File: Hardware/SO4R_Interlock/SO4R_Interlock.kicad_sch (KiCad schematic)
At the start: 165 parts, among them J1 12V, J2 USB-C 2.0 16P, J3 USB-C 2.0 16P, J4 USB-C 2.0 16P, J5 USB-C 2.0 16P, J6 Header 1x3, J7 RJ45_LED_Shielded, J8 8P8C_LED_Shielded_x4, Q1 2N7002, Q2 2N7002, Q3 2N7002, Q4 2N7002, U1 FT230XS, U10 TPD4E02B04DQA, U11 TPD4E02B04DQA, U12 TPD4E02B04DQA, U13 TPD4E02B04DQA, U2 FT230XS, U3 FT230XS, U4 FT230XS, U5 74LVC1G07, U6 74LVC1G07, U7 74LVC1G07, U8 BTS5200-4EKA, U9 AVR32DB48x-xPT

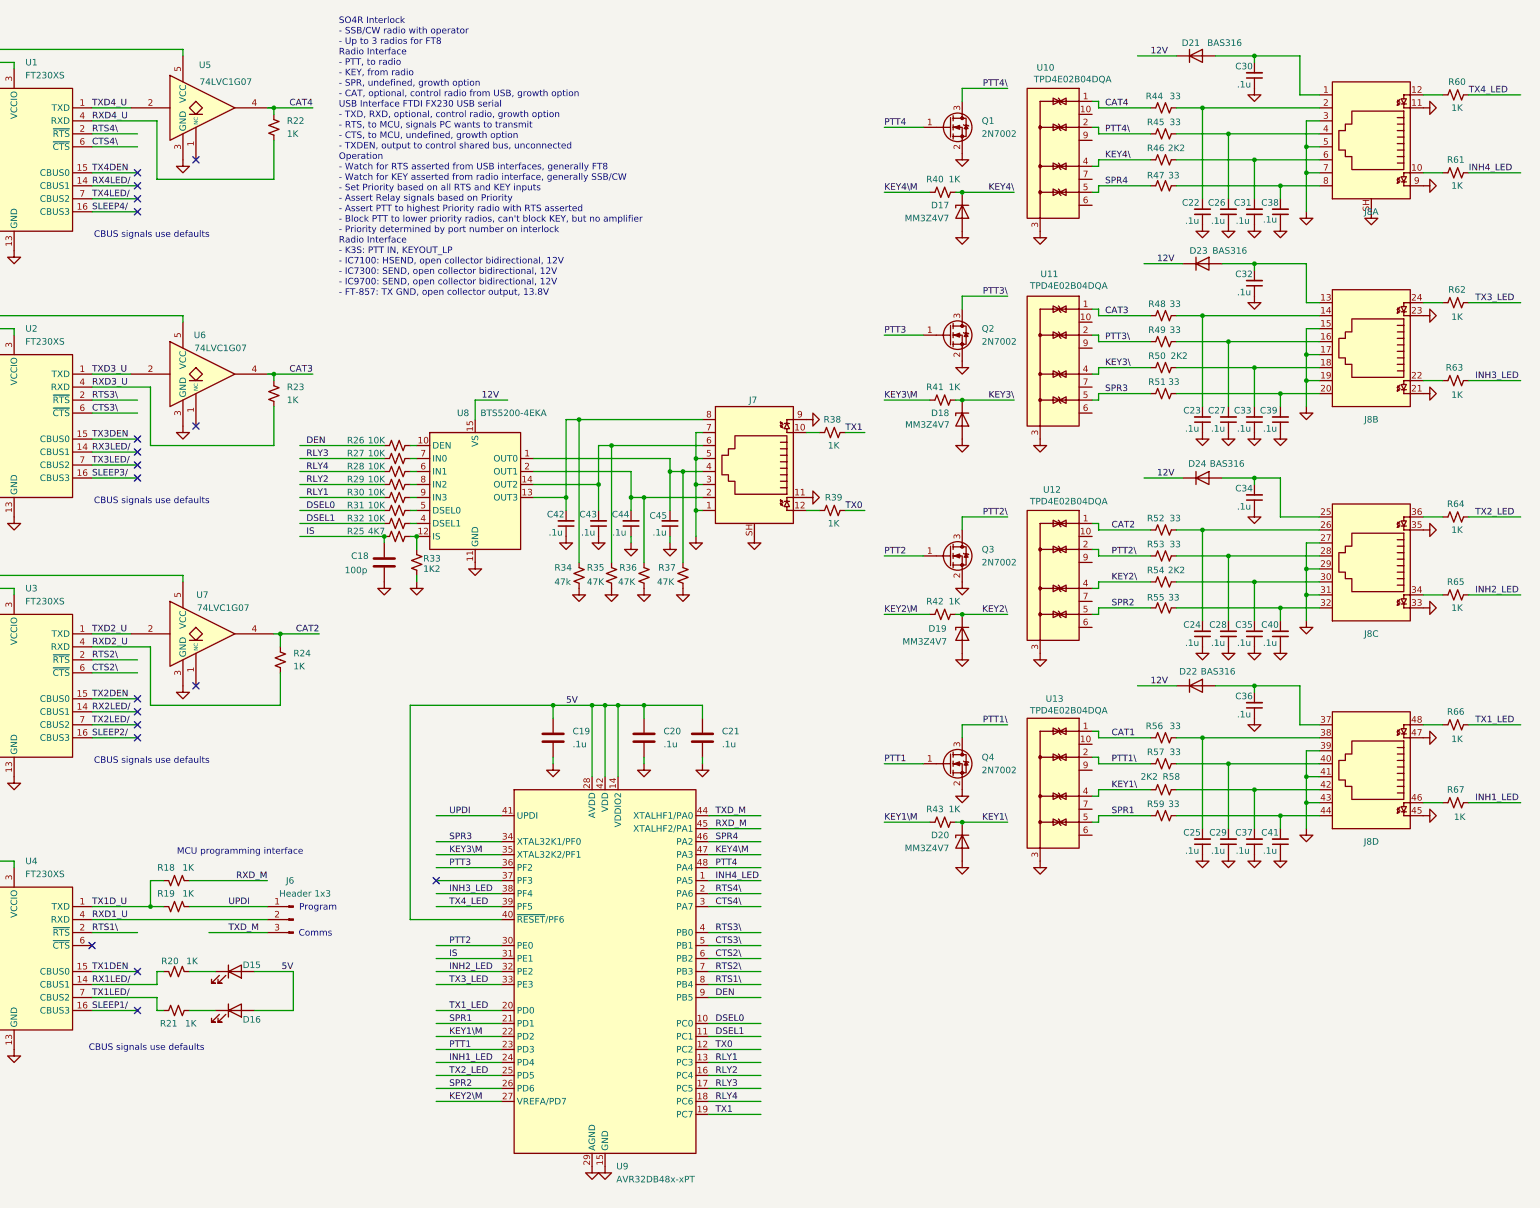
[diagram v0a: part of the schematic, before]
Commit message: Renamed LED signals for clarity Matching changes in Software and Hardware name
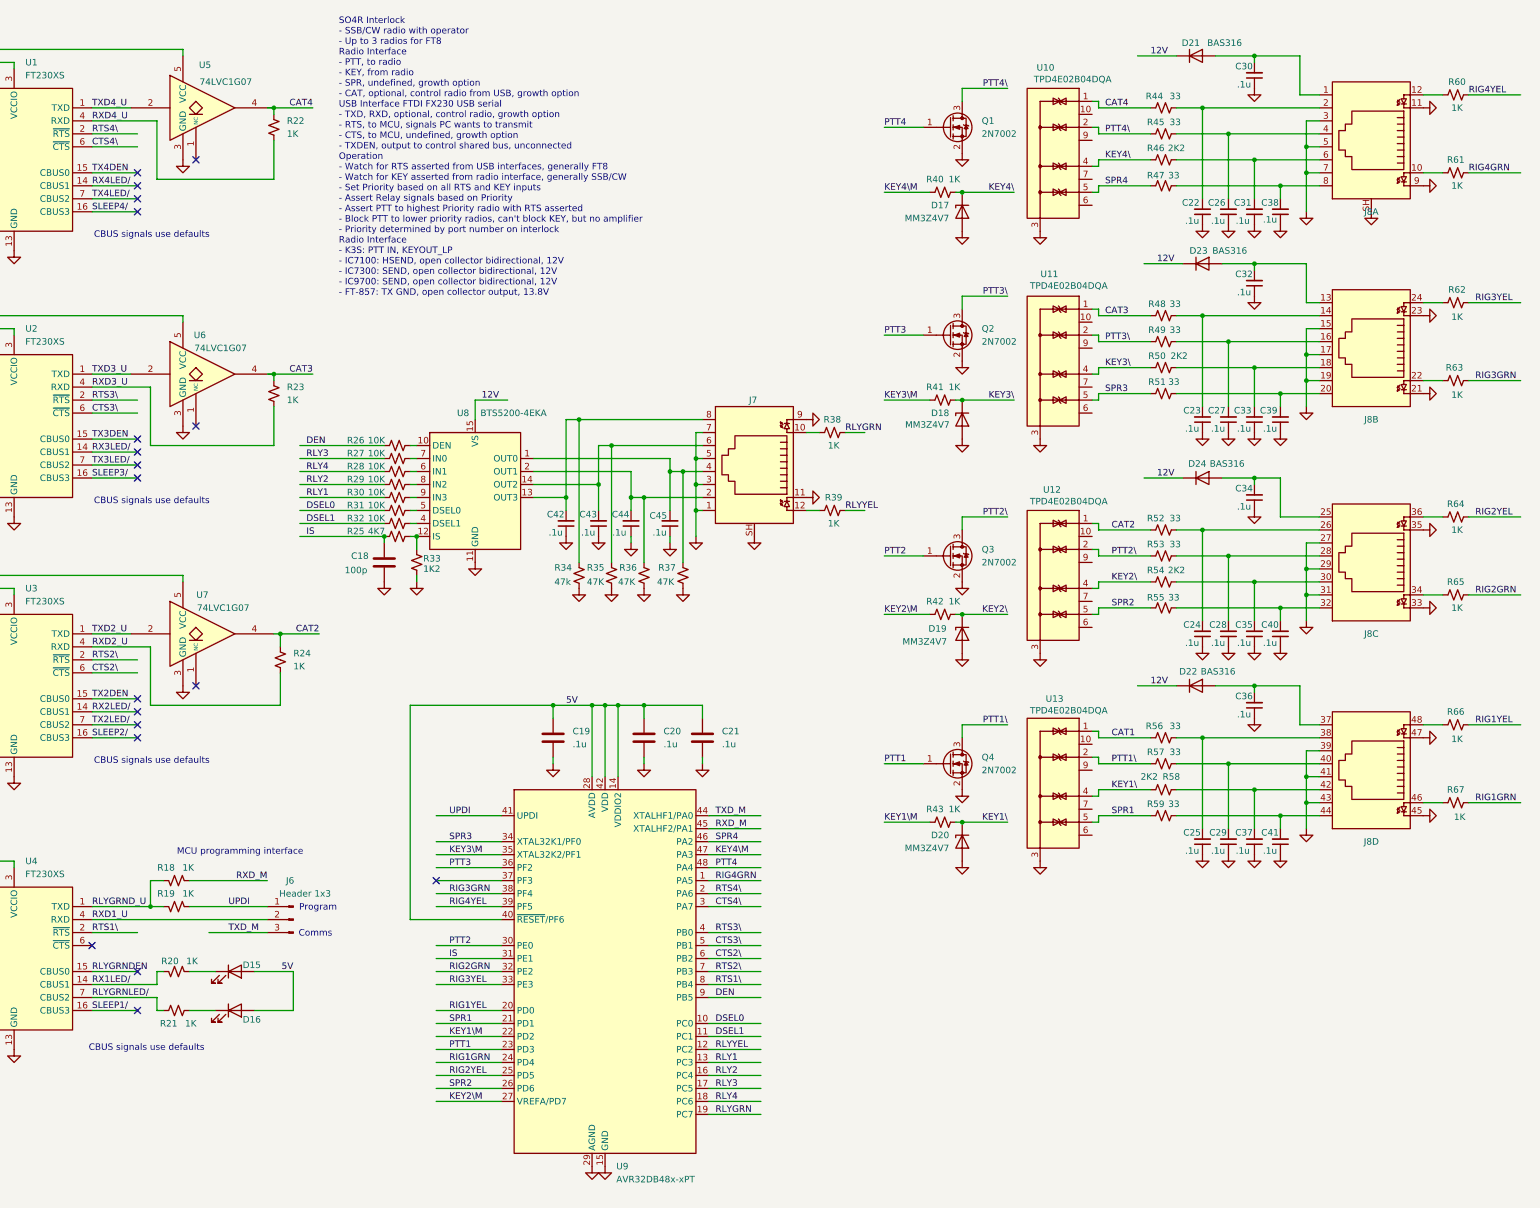
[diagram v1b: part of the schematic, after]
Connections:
- net INH1_LED renamed RIG1GRN
- net INH2_LED renamed RIG2GRN
- net INH3_LED renamed RIG3GRN
- net INH4_LED renamed RIG4GRN
- net TX0 renamed RLYYEL
- net TX1 renamed RLYGRN
- net TX1DEN renamed RLYGRNDEN
- net TX1D_U renamed RLYGRND_U
- net TX1LED/ renamed RLYGRNLED/
- net TX1_LED renamed RIG1YEL
- net TX2_LED renamed RIG2YEL
- net TX3_LED renamed RIG3YEL
- net TX4_LED renamed RIG4YEL
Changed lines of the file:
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@@
 		)
 	)
-	(label "TX1D_U"
+	(label "RLYGRND_U"
 		(at 138.43 190.5 0)
 		(effects
@@
 		)
 	)
-	(label "TX2_LED"
+	(label "RIG2YEL"
 		(at 408.94 114.3 0)
 		(effects
@@
 		)
 	)
-	(label "TX0"
+	(label "RLYYEL"
 		(at 285.75 113.03 0)
 		(effects
@@
 		)
 	)
-	(label "INH2_LED"
+	(label "RIG2GRN"
 		(at 208.28 203.2 0)
 		(effects
@@
 		)
 	)
-	(label "TX0"
+	(label "RLYYEL"
 		(at 260.35 218.44 0)
 		(effects
@@
 		)
 	)
-	(label "INH4_LED"
+	(label "RIG4GRN"
 		(at 260.35 185.42 0)
 		(effects
@@
 		)
 	)
-	(label "TX1"
+	(label "RLYGRN"
 		(at 285.75 97.79 0)
 		(effects
@@
 		)
 	)
-	(label "TX3_LED"
+	(label "RIG3YEL"
 		(at 208.28 205.74 0)
 		(effects
@@
 		)
 	)
-	(label "TX1DEN"
+	(label "RLYGRNDEN"
 		(at 138.43 203.2 0)
 		(effects
@@
 		)
 	)
-	(label "INH4_LED"
+	(label "RIG4GRN"
 		(at 407.67 46.99 0)
 		(effects
@@
 		)
 	)
-	(label "INH3_LED"
+	(label "RIG3GRN"
 		(at 408.94 87.63 0)
 		(effects
@@
 		)
 	)
-	(label "TX4_LED"
+	(label "RIG4YEL"
 		(at 407.67 31.75 0)
 		(effects
@@
 		)
 	)
-	(label "TX1_LED"
+	(label "RIG1YEL"
 		(at 208.28 210.82 0)
 		(effects
@@
 		)
 	)
-	(label "TX1"
+	(label "RLYGRN"
 		(at 260.35 231.14 0)
 		(effects
@@
 		)
 	)
-	(label "TX4_LED"
+	(label "RIG4YEL"
 		(at 208.28 190.5 0)
 		(effects
@@
 		)
 	)
-	(label "TX2_LED"
+	(label "RIG2YEL"
 		(at 208.28 223.52 0)
 		(effects
@@
 		)
 	)
-	(label "INH1_LED"
+	(label "RIG1GRN"
 		(at 408.94 170.18 0)
 		(effects
@@
 		)
 	)
-	(label "TX1LED/"
+	(label "RLYGRNLED/"
 		(at 138.43 208.28 0)
 		(effects
@@
 		)
 	)
-	(label "INH2_LED"
+	(label "RIG2GRN"
 		(at 408.94 129.54 0)
 		(effects
@@
 		)
 	)
-	(label "INH3_LED"
+	(label "RIG3GRN"
 		(at 208.28 187.96 0)
 		(effects
@@
 		)
 	)
-	(label "INH1_LED"
+	(label "RIG1GRN"
 		(at 208.28 220.98 0)
 		(effects
@@
 		)
 	)
-	(label "TX3_LED"
+	(label "RIG3YEL"
 		(at 408.94 72.39 0)
 		(effects
@@
 		)
 	)
-	(label "TX1_LED"
+	(label "RIG1YEL"
 		(at 408.94 154.94 0)
 		(effects

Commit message: still laying out pcb
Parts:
- removed D21, D22, D23, D24, D5: BAS316, Diode_SMD:D_SOD-323, symbol Diode:BAS316
- removed J2, J3, J4, J5: USB-C 2.0 16P, Interlock:USB_C_Receptacle_G-Switch_GT-USB-7010ASV, symbol Connector:USB_C_Receptacle_USB2.0_16P
- removed J6: Header 1x3, Connector_PinHeader_2.54mm:PinHeader_1x03_P2.54mm_Vertical, symbol Connector:Conn_01x03_Pin
- removed J8: 8P8C_LED_Shielded_x4, Connector_RJ:RJ45_Amphenol_RJHSE538X-04, symbol Interlock:8P8C_LED_Shielded_x4
- removed U10, U11, U12, U13: TPD4E02B04DQA, Package_SON:USON-10_2.5x1.0mm_P0.5mm, symbol Power_Protection:TPD4E02B04DQA
- added C26: .1u, Capacitor_SMD_Silkscreen:C_0402_1005Metric, symbol Device:C_Small
- added D1, D37, D38, D39, D40: RBQ161QS-40, Diode_SMD:D_0402_1005Metric, symbol Device:D_Schottky
- added D10: Green, LED_SMD:LED_0603_1608Metric, symbol Device:LED
- added D16, D17, D18, D19, D20, D21, D22, D23, D29, D30, D31, D32: Green, LED_SMD:LED_0805_2012Metric, symbol Device:LED
- added D26, D27, D28: MM3Z5V1, Diode_SMD:D_SOD-323F, symbol Diode:MM3Zxx
- added J2: USB_C_stacked, Interlock:CU3616SASCLA004-LF, symbol Interlock:USB-C_Stacked
- added J3: ~, Interlock:CU3616SASCLA004-LF, symbol Interlock:USB-C_Stacked
- added J5: Conn_Coaxial, Interlock:KLPX-0848A-2-B_KYC, symbol Connector:Conn_Coaxial
- added J6: 2041376-2, 2041376-2:TE_2041376-2, symbol RJ45_stacked_2x2_TE_2041376-2:2041376-2
- added Q1: 2N7002, Package_TO_SOT_SMD:SOT-23, symbol Transistor_FET:2N7002
- added R11, R12, R13, R14, R23, R24, R25, R26, R31, R32, R33, R34, R9: 1K, Resistor_SMD_Silkscreen:R_0402_1005Metric, symbol Device:R_Small_US
- added R35, R37, R39, R41: 4K7, Resistor_SMD_Silkscreen:R_0402_1005Metric, symbol Device:R_Small_US
- added R55: 33, Resistor_SMD_Silkscreen:R_0402_1005Metric, symbol Device:R_Small_US
- added SW1: SW_Wuerth_450301014042, Button_Switch_THT:SW_Slide-03_Wuerth-WS-SLTV_10x2.5x6.4_P2.54mm, symbol Switch:SW_Wuerth_450301014042
- C1, C14, C15, C16, C17, C18, C19: footprint Capacitor_SMD:C_0402_1005Metric -> Capacitor_SMD_Silkscreen:C_0402_1005Metric
- C10: renamed from C6; footprint Capacitor_SMD:C_0402_1005Metric -> Capacitor_SMD_Silkscreen:C_0402_1005Metric
- C11: renamed from C7; footprint Capacitor_SMD:C_0402_1005Metric -> Capacitor_SMD_Silkscreen:C_0402_1005Metric
- C12: renamed from C8; footprint Capacitor_SMD:C_0402_1005Metric -> Capacitor_SMD_Silkscreen:C_0402_1005Metric
- C13: renamed from C9; footprint Capacitor_SMD:C_0402_1005Metric -> Capacitor_SMD_Silkscreen:C_0402_1005Metric
- C2: renamed from C13; footprint Capacitor_SMD:C_0402_1005Metric -> Capacitor_SMD_Silkscreen:C_0402_1005Metric
- C20: renamed from C42; footprint Capacitor_SMD:C_0402_1005Metric -> Capacitor_SMD_Silkscreen:C_0402_1005Metric
- C21: renamed from C43; footprint Capacitor_SMD:C_0402_1005Metric -> Capacitor_SMD_Silkscreen:C_0402_1005Metric
- C22: renamed from C20; footprint Capacitor_SMD:C_0402_1005Metric -> Capacitor_SMD_Silkscreen:C_0402_1005Metric
- C23: renamed from C44; footprint Capacitor_SMD:C_0402_1005Metric -> Capacitor_SMD_Silkscreen:C_0402_1005Metric
- C24: renamed from C21; footprint Capacitor_SMD:C_0402_1005Metric -> Capacitor_SMD_Silkscreen:C_0402_1005Metric
- C25: renamed from C45; footprint Capacitor_SMD:C_0402_1005Metric -> Capacitor_SMD_Silkscreen:C_0402_1005Metric
- C27: renamed from C22; footprint Capacitor_SMD:C_0402_1005Metric -> Capacitor_SMD_Silkscreen:C_0402_1005Metric
- C28: renamed from C23; footprint Capacitor_SMD:C_0402_1005Metric -> Capacitor_SMD_Silkscreen:C_0402_1005Metric
- C29: renamed from C24; footprint Capacitor_SMD:C_0402_1005Metric -> Capacitor_SMD_Silkscreen:C_0402_1005Metric
- C3: renamed from C12; footprint Capacitor_SMD:C_0402_1005Metric -> Capacitor_SMD_Silkscreen:C_0402_1005Metric
- C30: renamed from C25; footprint Capacitor_SMD:C_0402_1005Metric -> Capacitor_SMD_Silkscreen:C_0402_1005Metric
- C31: renamed from C26; footprint Capacitor_SMD:C_0402_1005Metric -> Capacitor_SMD_Silkscreen:C_0402_1005Metric
- C32: renamed from C27; footprint Capacitor_SMD:C_0402_1005Metric -> Capacitor_SMD_Silkscreen:C_0402_1005Metric
- C33: renamed from C28; footprint Capacitor_SMD:C_0402_1005Metric -> Capacitor_SMD_Silkscreen:C_0402_1005Metric
- C34: renamed from C29; footprint Capacitor_SMD:C_0402_1005Metric -> Capacitor_SMD_Silkscreen:C_0402_1005Metric
- C35: renamed from C30; footprint Capacitor_SMD:C_0402_1005Metric -> Capacitor_SMD_Silkscreen:C_0402_1005Metric
- C36: renamed from C31; footprint Capacitor_SMD:C_0402_1005Metric -> Capacitor_SMD_Silkscreen:C_0402_1005Metric
- C37: renamed from C32; footprint Capacitor_SMD:C_0402_1005Metric -> Capacitor_SMD_Silkscreen:C_0402_1005Metric
- C38: renamed from C33; footprint Capacitor_SMD:C_0402_1005Metric -> Capacitor_SMD_Silkscreen:C_0402_1005Metric
- C39: renamed from C34; footprint Capacitor_SMD:C_0402_1005Metric -> Capacitor_SMD_Silkscreen:C_0402_1005Metric
- C4: renamed from C10; footprint Capacitor_SMD:C_0402_1005Metric -> Capacitor_SMD_Silkscreen:C_0402_1005Metric
- C40: renamed from C35; footprint Capacitor_SMD:C_0402_1005Metric -> Capacitor_SMD_Silkscreen:C_0402_1005Metric
- C41: renamed from C36; footprint Capacitor_SMD:C_0402_1005Metric -> Capacitor_SMD_Silkscreen:C_0402_1005Metric
- C42: renamed from C37; footprint Capacitor_SMD:C_0402_1005Metric -> Capacitor_SMD_Silkscreen:C_0402_1005Metric
- C43: renamed from C38; footprint Capacitor_SMD:C_0402_1005Metric -> Capacitor_SMD_Silkscreen:C_0402_1005Metric
- C44: renamed from C39; footprint Capacitor_SMD:C_0402_1005Metric -> Capacitor_SMD_Silkscreen:C_0402_1005Metric
- C45: renamed from C40; footprint Capacitor_SMD:C_0402_1005Metric -> Capacitor_SMD_Silkscreen:C_0402_1005Metric
- C46: renamed from C41; footprint Capacitor_SMD:C_0402_1005Metric -> Capacitor_SMD_Silkscreen:C_0402_1005Metric
- C5: renamed from C2; footprint Capacitor_SMD:C_0402_1005Metric -> Capacitor_SMD_Silkscreen:C_0402_1005Metric
- C6: renamed from C3; footprint Capacitor_SMD:C_0402_1005Metric -> Capacitor_SMD_Silkscreen:C_0402_1005Metric
- C7: renamed from C4; footprint Capacitor_SMD:C_0402_1005Metric -> Capacitor_SMD_Silkscreen:C_0402_1005Metric
- C8: renamed from C5; footprint Capacitor_SMD:C_0402_1005Metric -> Capacitor_SMD_Silkscreen:C_0402_1005Metric
- C9: renamed from C11; footprint Capacitor_SMD:C_0402_1005Metric -> Capacitor_SMD_Silkscreen:C_0402_1005Metric
- D11: renamed from D10; footprint Diode_SMD:D_SOD-323 -> Diode_SMD:D_SOD-523
- D12: renamed from D11; footprint Diode_SMD:D_SOD-323 -> Diode_SMD:D_SOD-523
- D13: renamed from D12; footprint Diode_SMD:D_SOD-323 -> Diode_SMD:D_SOD-523
- D14: renamed from D13; footprint Diode_SMD:D_SOD-323 -> Diode_SMD:D_SOD-523
- D2: renamed from D1; footprint Diode_SMD:D_SOD-323 -> Diode_SMD:D_SOD-523
- D3: renamed from D2; footprint Diode_SMD:D_SOD-323 -> Diode_SMD:D_SOD-523
- D33: renamed from D17; value MM3Z4V7 -> MM3Z5V1; footprint Diode_SMD:D_SOD-323 -> Diode_SMD:D_SOD-523
- D34: renamed from D18; value MM3Z4V7 -> MM3Z5V1; footprint Diode_SMD:D_SOD-323 -> Diode_SMD:D_SOD-523
- D35: renamed from D19; value MM3Z4V7 -> MM3Z5V1; footprint Diode_SMD:D_SOD-323 -> Diode_SMD:D_SOD-523
- D36: renamed from D20; value MM3Z4V7 -> MM3Z5V1; footprint Diode_SMD:D_SOD-323 -> Diode_SMD:D_SOD-523
- D4: renamed from D3; footprint Diode_SMD:D_SOD-323 -> Diode_SMD:D_SOD-523
- D5: renamed from D4; footprint Diode_SMD:D_SOD-323 -> Diode_SMD:D_SOD-523
- R1: footprint Resistor_SMD:R_0402_1005Metric -> Resistor_SMD_Silkscreen:R_0402_1005Metric; symbol Device:R_US -> Device:R_Small_US
- R10: renamed from R9; footprint Resistor_SMD:R_0402_1005Metric -> Resistor_SMD_Silkscreen:R_0402_1005Metric
- R15: renamed from R10; footprint Resistor_SMD:R_0402_1005Metric -> Resistor_SMD_Silkscreen:R_0402_1005Metric
- R16: renamed from R11; footprint Resistor_SMD:R_0402_1005Metric -> Resistor_SMD_Silkscreen:R_0402_1005Metric
- R17: renamed from R12; footprint Resistor_SMD:R_0402_1005Metric -> Resistor_SMD_Silkscreen:R_0402_1005Metric
- R18: renamed from R13; footprint Resistor_SMD:R_0402_1005Metric -> Resistor_SMD_Silkscreen:R_0402_1005Metric
- R19: renamed from R14; footprint Resistor_SMD:R_0402_1005Metric -> Resistor_SMD_Silkscreen:R_0402_1005Metric
- R2, R3, R4, R5, R6, R7, R8: footprint Resistor_SMD:R_0402_1005Metric -> Resistor_SMD_Silkscreen:R_0402_1005Metric
- R20: renamed from R15; footprint Resistor_SMD:R_0402_1005Metric -> Resistor_SMD_Silkscreen:R_0402_1005Metric
- R21: renamed from R16; footprint Resistor_SMD:R_0402_1005Metric -> Resistor_SMD_Silkscreen:R_0402_1005Metric
- R22: renamed from R17; footprint Resistor_SMD:R_0402_1005Metric -> Resistor_SMD_Silkscreen:R_0402_1005Metric
- R27: renamed from R18; footprint Resistor_SMD:R_0402_1005Metric -> Resistor_SMD_Silkscreen:R_0402_1005Metric
- R28: renamed from R19; footprint Resistor_SMD:R_0402_1005Metric -> Resistor_SMD_Silkscreen:R_0402_1005Metric
- R29: renamed from R20; footprint Resistor_SMD:R_0402_1005Metric -> Resistor_SMD_Silkscreen:R_0402_1005Metric
- R30: renamed from R21; footprint Resistor_SMD:R_0402_1005Metric -> Resistor_SMD_Silkscreen:R_0402_1005Metric
- R36: renamed from R22; value 1K -> 4K7; footprint Resistor_SMD:R_0402_1005Metric -> Resistor_SMD_Silkscreen:R_0402_1005Metric
- R38: renamed from R23; value 1K -> 4K7; footprint Resistor_SMD:R_0402_1005Metric -> Resistor_SMD_Silkscreen:R_0402_1005Metric
- R40: renamed from R24; value 1K -> 4K7; footprint Resistor_SMD:R_0402_1005Metric -> Resistor_SMD_Silkscreen:R_0402_1005Metric
- R42: renamed from R26; footprint Resistor_SMD:R_0402_1005Metric -> Resistor_SMD_Silkscreen:R_0402_1005Metric
- R43: renamed from R27; footprint Resistor_SMD:R_0402_1005Metric -> Resistor_SMD_Silkscreen:R_0402_1005Metric
- R44: renamed from R28; footprint Resistor_SMD:R_0402_1005Metric -> Resistor_SMD_Silkscreen:R_0402_1005Metric
- R45: renamed from R29; footprint Resistor_SMD:R_0402_1005Metric -> Resistor_SMD_Silkscreen:R_0402_1005Metric
- R46: renamed from R30; footprint Resistor_SMD:R_0402_1005Metric -> Resistor_SMD_Silkscreen:R_0402_1005Metric
- R47: renamed from R31; footprint Resistor_SMD:R_0402_1005Metric -> Resistor_SMD_Silkscreen:R_0402_1005Metric
- R48: renamed from R32; footprint Resistor_SMD:R_0402_1005Metric -> Resistor_SMD_Silkscreen:R_0402_1005Metric
- R49: renamed from R25; footprint Resistor_SMD:R_0402_1005Metric -> Resistor_SMD_Silkscreen:R_0402_1005Metric
- R50: renamed from R33; footprint Resistor_SMD:R_0402_1005Metric -> Resistor_SMD_Silkscreen:R_0402_1005Metric
- R51: renamed from R34; value 47k -> 4K7; footprint Resistor_SMD:R_0402_1005Metric -> Resistor_SMD_Silkscreen:R_0402_1005Metric
- R52: renamed from R35; footprint Resistor_SMD:R_0402_1005Metric -> Resistor_SMD_Silkscreen:R_0402_1005Metric
- R53: renamed from R36; footprint Resistor_SMD:R_0402_1005Metric -> Resistor_SMD_Silkscreen:R_0402_1005Metric
- R54: renamed from R37; footprint Resistor_SMD:R_0402_1005Metric -> Resistor_SMD_Silkscreen:R_0402_1005Metric
- R56: renamed from R38; footprint Resistor_SMD:R_0402_1005Metric -> Resistor_SMD_Silkscreen:R_0402_1005Metric
- R57: renamed from R39; footprint Resistor_SMD:R_0402_1005Metric -> Resistor_SMD_Silkscreen:R_0402_1005Metric
- R58: renamed from R40; footprint Resistor_SMD:R_0402_1005Metric -> Resistor_SMD_Silkscreen:R_0402_1005Metric
- R59: renamed from R41; footprint Resistor_SMD:R_0402_1005Metric -> Resistor_SMD_Silkscreen:R_0402_1005Metric
- R60: renamed from R42; footprint Resistor_SMD:R_0402_1005Metric -> Resistor_SMD_Silkscreen:R_0402_1005Metric
- R61: renamed from R43; footprint Resistor_SMD:R_0402_1005Metric -> Resistor_SMD_Silkscreen:R_0402_1005Metric
- R62: renamed from R44; footprint Resistor_SMD:R_0402_1005Metric -> Resistor_SMD_Silkscreen:R_0402_1005Metric
- R63: renamed from R45; footprint Resistor_SMD:R_0402_1005Metric -> Resistor_SMD_Silkscreen:R_0402_1005Metric
- R64: renamed from R46; footprint Resistor_SMD:R_0402_1005Metric -> Resistor_SMD_Silkscreen:R_0402_1005Metric
- R65: renamed from R47; footprint Resistor_SMD:R_0402_1005Metric -> Resistor_SMD_Silkscreen:R_0402_1005Metric
- R66: renamed from R48; footprint Resistor_SMD:R_0402_1005Metric -> Resistor_SMD_Silkscreen:R_0402_1005Metric
- R67: renamed from R49; footprint Resistor_SMD:R_0402_1005Metric -> Resistor_SMD_Silkscreen:R_0402_1005Metric
- R68: renamed from R50; footprint Resistor_SMD:R_0402_1005Metric -> Resistor_SMD_Silkscreen:R_0402_1005Metric
- R69: renamed from R51; footprint Resistor_SMD:R_0402_1005Metric -> Resistor_SMD_Silkscreen:R_0402_1005Metric
- R70: renamed from R52; footprint Resistor_SMD:R_0402_1005Metric -> Resistor_SMD_Silkscreen:R_0402_1005Metric
- R71: renamed from R53; footprint Resistor_SMD:R_0402_1005Metric -> Resistor_SMD_Silkscreen:R_0402_1005Metric
- R72: renamed from R54; footprint Resistor_SMD:R_0402_1005Metric -> Resistor_SMD_Silkscreen:R_0402_1005Metric
- R73: renamed from R55; footprint Resistor_SMD:R_0402_1005Metric -> Resistor_SMD_Silkscreen:R_0402_1005Metric
- R74: renamed from R56; footprint Resistor_SMD:R_0402_1005Metric -> Resistor_SMD_Silkscreen:R_0402_1005Metric
- R75: renamed from R57; footprint Resistor_SMD:R_0402_1005Metric -> Resistor_SMD_Silkscreen:R_0402_1005Metric
- R76: renamed from R58; footprint Resistor_SMD:R_0402_1005Metric -> Resistor_SMD_Silkscreen:R_0402_1005Metric
- R77: renamed from R59; footprint Resistor_SMD:R_0402_1005Metric -> Resistor_SMD_Silkscreen:R_0402_1005Metric
- R78: renamed from R61; footprint Resistor_SMD:R_0402_1005Metric -> Resistor_SMD_Silkscreen:R_0402_1005Metric
- R79: renamed from R60; footprint Resistor_SMD:R_0402_1005Metric -> Resistor_SMD_Silkscreen:R_0402_1005Metric
- R80: renamed from R62; footprint Resistor_SMD:R_0402_1005Metric -> Resistor_SMD_Silkscreen:R_0402_1005Metric
- R81: renamed from R63; footprint Resistor_SMD:R_0402_1005Metric -> Resistor_SMD_Silkscreen:R_0402_1005Metric
- R82: renamed from R64; footprint Resistor_SMD:R_0402_1005Metric -> Resistor_SMD_Silkscreen:R_0402_1005Metric
- R83: renamed from R65; footprint Resistor_SMD:R_0402_1005Metric -> Resistor_SMD_Silkscreen:R_0402_1005Metric
- R84: renamed from R67; footprint Resistor_SMD:R_0402_1005Metric -> Resistor_SMD_Silkscreen:R_0402_1005Metric
- R85: renamed from R66; footprint Resistor_SMD:R_0402_1005Metric -> Resistor_SMD_Silkscreen:R_0402_1005Metric
- U8: footprint Interlock:Infineon_PG-DSO-14-48-EP -> Package_SO:Infineon_PG-DSO-14-48
- renumbered D14 to D15, D15 to D24, D16 to D25, D9 to D6, D6 to D7, D7 to D8, D8 to D9, J7 to J4, Q1 to Q2, Q2 to Q3, Q3 to Q4, Q4 to Q5
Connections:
- net 12V: now also D1.1 (K), D37.1 (K), D38.1 (K), D39.1 (K), D40.1 (K), R9.2
- net 5V: now also R11.1, R12.1, R13.1, R14.1, R35.1, R37.1, R39.1, R41.1; no longer U9.40 (~{RESET}/PF6)
- net CAT2: now also R39.2
- net CAT3: now also R37.2
- net CAT4: now also R35.2
- net CTS2\: now also U9.24 (PD4); no longer U9.6 (PB2)
- net CTS3\: now also U9.22 (PD2); no longer U9.5 (PB1)
- net CTS4\: now also U9.20 (PD0); no longer U9.3 (PA7)
- net DEN: now also U9.32 (PE2); no longer U9.9 (PB5)
- net DSEL0: now also U9.37 (PF3); no longer U9.10 (PC0)
- net DSEL1: now also U9.38 (PF4); no longer U9.11 (PC1)
- net GND: now also C26.1, D10.1 (K), D20.1 (K), D21.1 (K), D22.1 (K), D23.1 (K), D26.2 (A), D27.1 (K), D28.2 (A), D29.1 (K), D30.1 (K), D31.1 (K), D32.1 (K), J2.A12a (GND), J2.A12b (GND), J2.A1a (GND), J2.A1b (GND), J2.B12a (GND), J2.B12b (GND), J2.B1a (GND), J2.B1b (GND), J2.S1 (SHIELD), J3.A12a (GND), J3.A12b (GND), J3.A1a (GND), J3.A1b (GND), J3.B12a (GND), J3.B12b (GND), J3.B1a (GND), J3.B1b (GND), J3.S1 (SHIELD), J5.2 (Ext), J6.A3, J6.A5, J6.A7, J6.B3, J6.B5, J6.B7, J6.C3, J6.C5, J6.C7, J6.D3, J6.D5, J6.D7, J6.GK_A, J6.GK_B, J6.GK_C, J6.GK_D, J6.S1 (SHIELD), J6.S2 (SHIELD__1), J6.S3 (SHIELD__2), J6.S4 (SHIELD__3), J6.YK_A, J6.YK_B, J6.YK_C, J6.YK_D, Q1.2 (S)
- net KEY1\M: now also U9.11 (PC1); no longer U9.22 (PD2)
- net KEY2\M: now also U9.5 (PB1); no longer U9.27 (VREFA/PD7)
- net KEY3\M: now also U9.17 (PC5); no longer U9.35 (XTAL32K2/PF1)
- net KEY4\M: now also U9.1 (PA5); no longer U9.47 (PA3)
- net PTT1: now also U9.12 (PC2); no longer U9.23 (PD3)
- net PTT2: now also R82.2, U9.6 (PB2), R24.1; no longer U9.30 (PE0)
- net PTT3: now also R80.2, U9.16 (PC4), R25.1; no longer U9.36 (PF2)
- net PTT4: now also R78.2, R26.1
- net RIG1GRN: now also U9.8 (PB4), R23.1; no longer U9.24 (PD4)
- net RIG1YEL: now also U9.13 (PC3), R31.1; no longer U9.20 (PD0)
- net RIG2YEL: now also R83.2, U9.7 (PB3), R32.1; no longer R82.2, U9.25 (PD5)
- net RIG3YEL: now also R81.2, U9.19 (PC7), R33.1; no longer R80.2, U9.33 (PE3)
- net RIG4YEL: now also U9.46 (PA2), R34.1; no longer U9.39 (PF5)
- net RLY1: now also U9.33 (PE3); no longer U9.13 (PC3)
- net RLY2: now also U9.34 (XTAL32K1/PF0); no longer U9.16 (PC4)
- net RLY3: now also U9.35 (XTAL32K2/PF1); no longer U9.17 (PC5)
- net RLY4: now also U9.36 (PF2); no longer U9.18 (PC6)
- net RLYGRN: now also U9.39 (PF5); no longer U9.19 (PC7)
- net RLYYEL: now also U9.30 (PE0); no longer U9.12 (PC2)
- net RTS1\: now also U9.26 (PD6); no longer U9.8 (PB4)
- net RTS2\: now also U9.25 (PD5); no longer U9.7 (PB3)
- net RTS3\: now also U9.23 (PD3); no longer U9.4 (PB0)
- net RTS4\: now also U9.21 (PD1); no longer U9.2 (PA6)
- net RXD1_U: now also SW1.1 (B)
- net RXD2_U: now also D28.1 (K)
- net RXD3_U: now also D27.2 (A)
- net RXD4_U: now also D26.1 (K)
- net SPR1: now also U9.10 (PC0); no longer U9.21 (PD1)
- net SPR2: now also U9.4 (PB0); no longer U9.26 (PD6)
- net SPR3: now also U9.18 (PC6); no longer U9.34 (XTAL32K1/PF0)
- net SPR4: now also U9.2 (PA6); no longer U9.46 (PA2)
- net TXD_M: now also SW1.2 (C)
- net UPDI: now also SW1.3 (A)
- net at R3.2: now also J2.A5b (CC1)
- net at C28.2, R66.2: now also J6.B2
- net at C37.2: now also D39.2 (A), J6.B1
- net at C32.2, R67.2: now also J6.B4
- net at C38.2, R68.1: now also J6.B6
- net at C44.2, R69.2: now also J6.B8
- net at R81.1: now also J6.YA_B
- net at R80.1: now also J6.GA_B
- net at C8.1, D14.1 (K), R21.2: now also J3.A7b (D-), J3.B7b (D-)
- net at C1.1, J1.1 (In): now also D1.2 (A)
- net at C11.1, D3.1 (K), R18.2: now also J2.A6b (D+), J2.B6b (D+)
- net at C39.2: now also D40.2 (A), J6.C1
- net at C29.2, R70.2: now also J6.C2
- net at C33.2, R71.2: now also J6.C4
- net at C40.2, R72.1: now also J6.C6
- net at C45.2, R73.2: now also J6.C8
- net at R83.1: now also J6.YA_C
- net at R82.1: now also J6.GA_C
- net at C31.2, R63.2: now also J6.A4
- net at C30.2, R74.2: now also J6.D2
- net at C13.1, D5.1 (K), R22.2: now also J3.A6b (D+), J3.B6b (D+)
- net at C34.2, R75.2: now also J6.D4
- net at C5.1, D11.1 (K), R15.2: now also J2.A7a (D-), J2.B7a (D-)
- net at R1.2: now also J2.A5a (CC1)
- net at C43.2, R65.2: now also J6.A8
- net at C41.2: now also D38.2 (A), J6.D1
- net at R79.1: now also J6.YA_A
- net at FB1.1: now also J2.A4b (VBUS), J2.A9b (VBUS), J2.B4b (VBUS), J2.B9b (VBUS)
- net at C10.1, D2.1 (K), R16.2: now also J2.A6a (D+), J2.B6a (D+)
- net at C42.2, R76.1: now also J6.D6
- net at C6.1, D12.1 (K), R17.2: now also J2.A7b (D-), J2.B7b (D-)
- net at R4.2: now also J2.B5b (CC2)
- net at C12.1, D4.1 (K), R20.2: now also J3.A6a (D+), J3.B6a (D+)
- net at FB4.1: now also J2.A4a (VBUS), J2.A9a (VBUS), J2.B4a (VBUS), J2.B9a (VBUS)
- net at R2.2: now also J2.B5a (CC2)
- net at C46.2, R77.2: now also J6.D8
- net at R85.1: now also J6.YA_D
- net at C7.1, D13.1 (K), R19.2: now also J3.A7a (D-), J3.B7a (D-)
- net at C27.2, R62.2: now also J6.A2
- net at R8.2: now also J3.B5b (CC2)
- net at C35.2: now also D37.2 (A), J6.A1
- net at R84.1: now also J6.GA_D
- net at R78.1: now also J6.GA_A
- net at C36.2, R64.1: now also J6.A6
- net at R5.2: now also J3.A5a (CC1)
- net at FB2.1: now also J3.A4a (VBUS), J3.A9a (VBUS), J3.B4a (VBUS), J3.B9a (VBUS)
- net at R6.2: now also J3.B5a (CC2)
- net at FB3.1: now also J3.A4b (VBUS), J3.A9b (VBUS), J3.B4b (VBUS), J3.B9b (VBUS)
- net at R7.2: now also J3.A5b (CC1)
- removed net RIG2GRN: R83.2, U9.32 (PE2)
- removed net RIG3GRN: R81.2, U9.38 (PF4)
- removed net RIG4GRN: R78.2, U9.1 (PA5)
- net RLYGRNDEN renamed TX1DEN
- net RLYGRND_U renamed TXD1_U
- net RLYGRNLED/ renamed TX1LED/
- new net: D10.2 (A), R9.1
- new net: D29.2 (A), R31.2
- new net: D30.2 (A), R32.2
- new net: D18.2 (A), R13.2
- new net: D31.2 (A), R33.2
- new net: D22.2 (A), R25.2
- new net: D23.2 (A), R26.2
- new net: R41.2, U9.40 (~{RESET}/PF6)
- new net: D17.2 (A), R12.2
- new net: D21.2 (A), R24.2
- new net: D32.2 (A), R34.2
- new net: Q1.3 (D), R55.1
- new net: D20.2 (A), R23.2
- new net: D19.2 (A), R14.2
- new net: D16.2 (A), R11.2
- new net: C26.2, J5.1 (In), R55.2
- new net PA_KEY: Q1.1 (G)
- new net RTS1/: D16.1 (K)
- new net RTS2/: D17.1 (K)
- new net RTS3/: D18.1 (K)
- new net RTS4/: D19.1 (K)
- no-connect marks 27 -> 31
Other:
- note added: "SO4R Interlock - SSB/CW radio with operator - Up to 3 radios for FT8 Radio Interface - PTT, to radio - KEY, from radio - CAT, optional, control radio from USB, growth option - SPR, undefined, growth option USB Interface FTDI FX230 USB serial - TXD, RXD, converted to CAT, 5V open collector - RTS, to MCU, signals PC wants to transmit - CTS, from MCU, growth option Operation - Watch for RTS asserted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"
- note removed: "SO4R Interlock - SSB/CW radio with operator - Up to 3 radios for FT8 Radio Interface - PTT, to radio - KEY, from radio - SPR, undefined, growth option - CAT, optional, control radio from USB, growth option USB Interface FTDI FX230 USB serial - TXD, RXD, optional, control radio, growth option - RTS, to MCU, signals PC wants to transmit - CTS, to MCU, undefined, growth option - TXDEN, output to con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"
- moved on the sheet: C18, C2, C20, C21, C23, C25, C27, C28, C29, C3, C30, C31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

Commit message: PCB layout ready for checking
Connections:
- net 5V: now also R29.2, R30.2; no longer D24.2 (A), D25.2 (A)
- net PA_KEY: now also U9.27 (VREFA/PD7)
- net RX1LED/: now also D25.1 (K); no longer R29.1
- net TX1LED/: now also D24.1 (K); no longer R30.1
- new net: D24.2 (A), R29.1
- new net: D25.2 (A), R30.1
- no-connect marks 31 -> 30
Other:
- note added: "Front Panel LEDs"
- moved on the sheet: C1, D1, D10, D15, D16, D17, D18, D19, D20, D21, D22, D23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
